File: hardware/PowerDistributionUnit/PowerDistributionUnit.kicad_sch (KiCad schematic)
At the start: 99 parts, among them J1 973582101, J2 973582100, J3 973582101, J4 973582100, Q1 SQJ141ELP, Q16 CSD18511Q5A, SW1 SW_Push, U1 TPS25983, U2 AD5258, U3 NUCLEO_LK43C

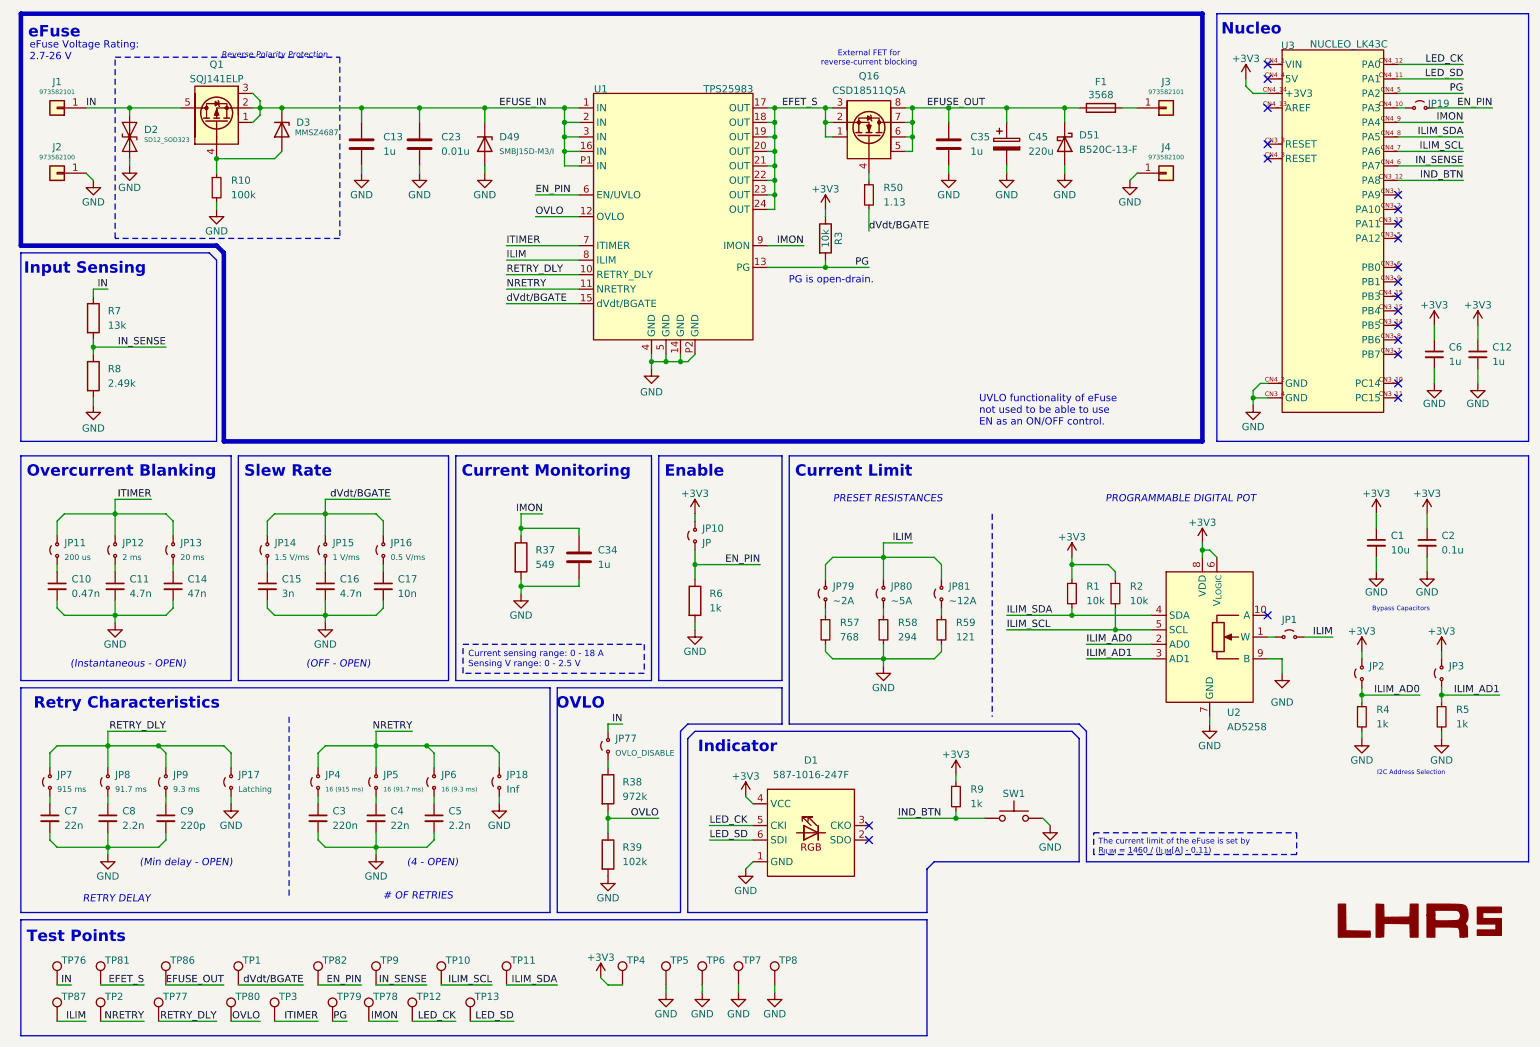
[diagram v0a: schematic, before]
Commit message: added separate power ground
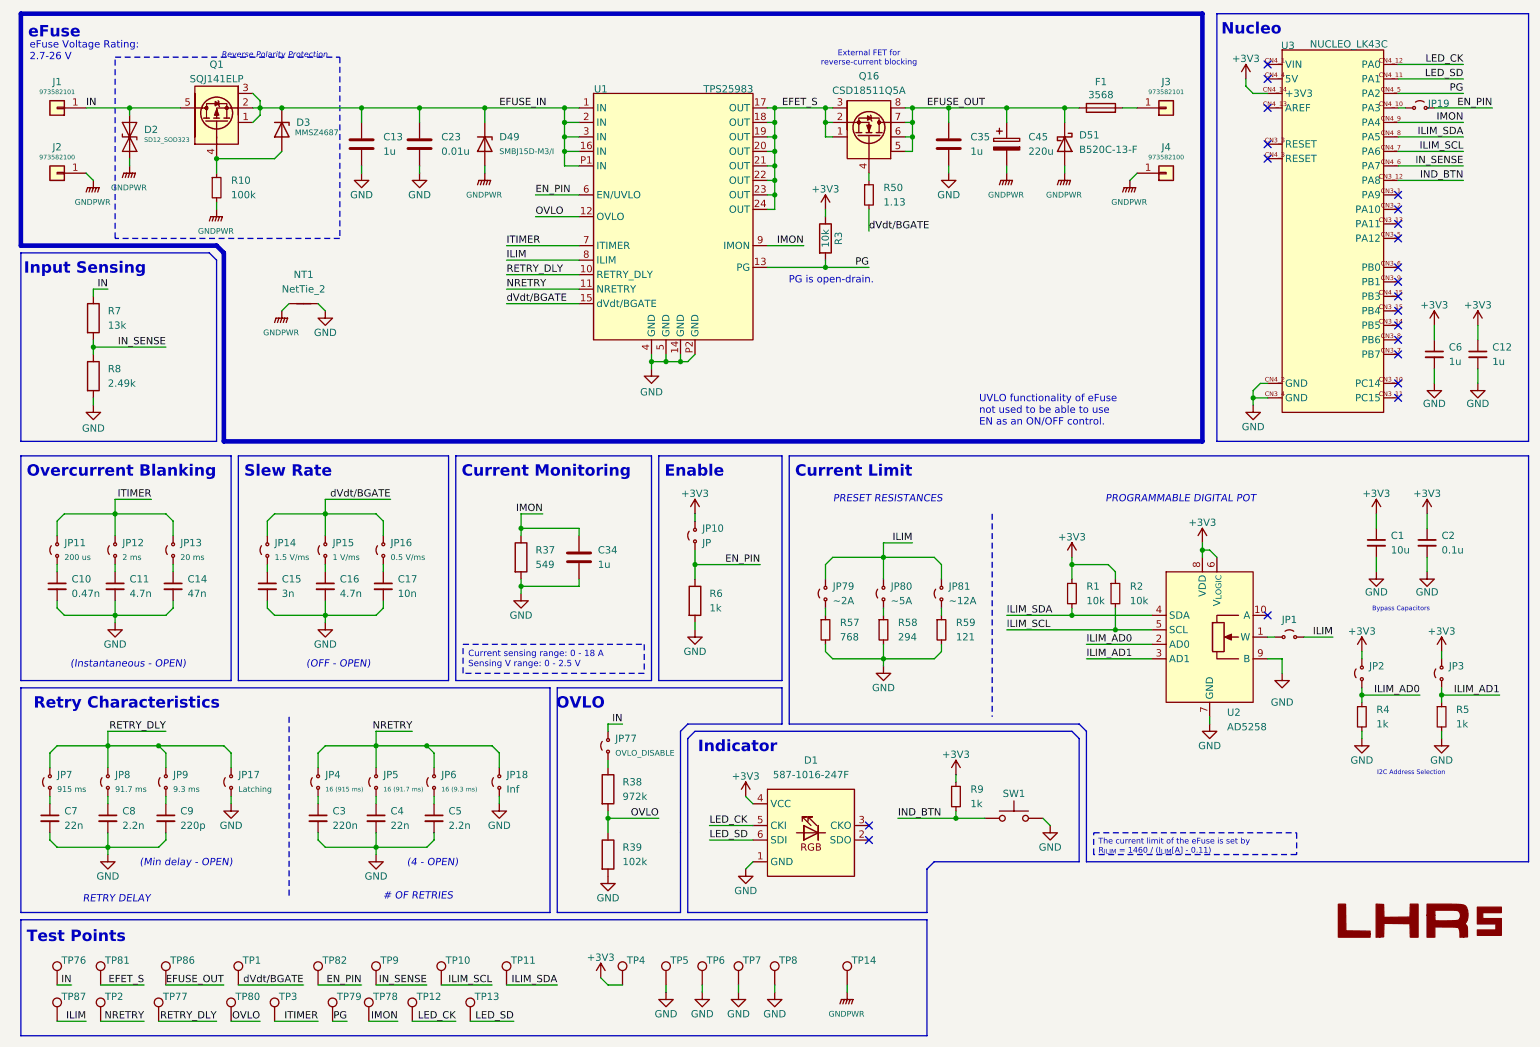
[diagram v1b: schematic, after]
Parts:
- added NT1: NetTie_2, symbol Device:NetTie_2
- added TP14: GND, symbol Connector:TestPoint
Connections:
- net GND: now also NT1.2; no longer C45.2, D2.1 (A1), D49.2 (A), D51.2 (A), J2.1 (Pin_1), J4.1 (Pin_1), R10.2
- new net GNDPWR: C45.2, D2.1 (A1), D49.2 (A), D51.2 (A), J2.1 (Pin_1), J4.1 (Pin_1), NT1.1, R10.2, TP14.1

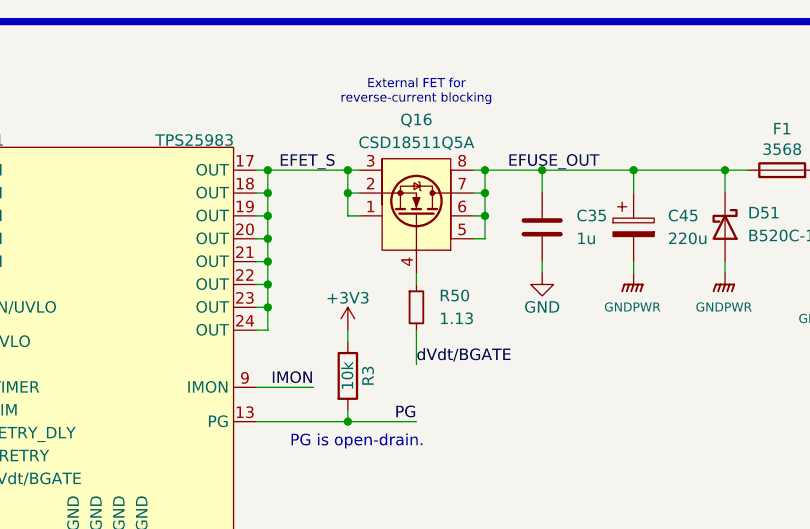
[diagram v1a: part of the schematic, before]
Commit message: footprint assignment, fixed rev current blocking fet symbol not matching generic footprint pins (replaced with generic mosfet symbol), fixed efuse pads pin numbers not lining up to footprint, added efuse footprint 3d model, added led footprint, imported footprints to pcb editor
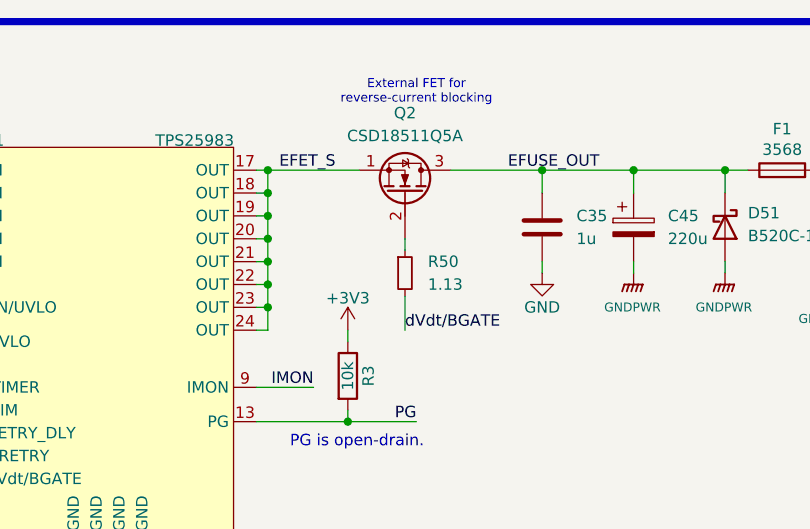
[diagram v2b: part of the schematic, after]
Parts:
- removed Q16: CSD18511Q5A, Package_SON:VSONP-8-1EP_5x6_P1.27mm, symbol PowerDistributionUnitLib:CSD18511Q5A
- added Q2: CSD18511Q5A, Package_SON:VSONP-8-1EP_5x6_P1.27mm, symbol Device:Q_NMOS_SGD
- C1, C10, C11, C12, C13, C14, C15, C16, C17, C2, C23, C3, C34, C35, C4, C5, C6, C7, C8, C9: footprint (none) -> Capacitor_SMD:C_0805_2012Metric
- C45: footprint Capacitor_SMD:CP_Elec_10x10.5 -> Capacitor_SMD:CP_Elec_10x12.6
- JP1, JP10, JP11, JP12, JP13, JP14, JP15, JP16, JP17, JP18, JP19, JP2, JP3, JP4, JP5, JP6, JP7, JP77, JP79, JP8, JP80, JP81, JP9: footprint (none) -> Connector_PinHeader_2.54mm:PinHeader_1x02_P2.54mm_Vertical
- NT1: footprint (none) -> NetTie:NetTie-2_SMD_Pad0.5mm
- R1, R10, R2, R3, R37, R38, R39, R4, R5, R50, R57, R58, R59, R6, R7, R8, R9: footprint (none) -> Resistor_SMD:R_0805_2012Metric
- TP1, TP2, TP3, TP76, TP77, TP78, TP79, TP80, TP81, TP82, TP86, TP87: footprint (none) -> TestPoint:TestPoint_Pad_D1.0mm
- TP10: value VIN -> ILIM_SCL; footprint (none) -> Connector_PinHeader_2.54mm:PinHeader_1x01_P2.54mm_Vertical
- TP11: value VIN -> ILIM_SDA; footprint (none) -> Connector_PinHeader_2.54mm:PinHeader_1x01_P2.54mm_Vertical
- TP12: value VIN -> LED_CK; footprint (none) -> Connector_PinHeader_2.54mm:PinHeader_1x01_P2.54mm_Vertical
- TP13: value VIN -> LED_SD; footprint (none) -> Connector_PinHeader_2.54mm:PinHeader_1x01_P2.54mm_Vertical
- TP14, TP4, TP5, TP6, TP7, TP8: footprint (none) -> Connector_PinHeader_2.54mm:PinHeader_1x01_P2.54mm_Vertical
- TP9: value VIN -> IN_SENSE; footprint (none) -> TestPoint:TestPoint_Pad_D1.0mm
- U3: footprint (none) -> PowerDistributionUnitLib:MODULE_NUCLEO-L432KC
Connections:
- net EFET_S: now also Q2.1 (S)
- net EFUSE_OUT: now also Q2.3 (D)
- net at R50.1: now also Q2.2 (G)
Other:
- moved on the sheet: R50

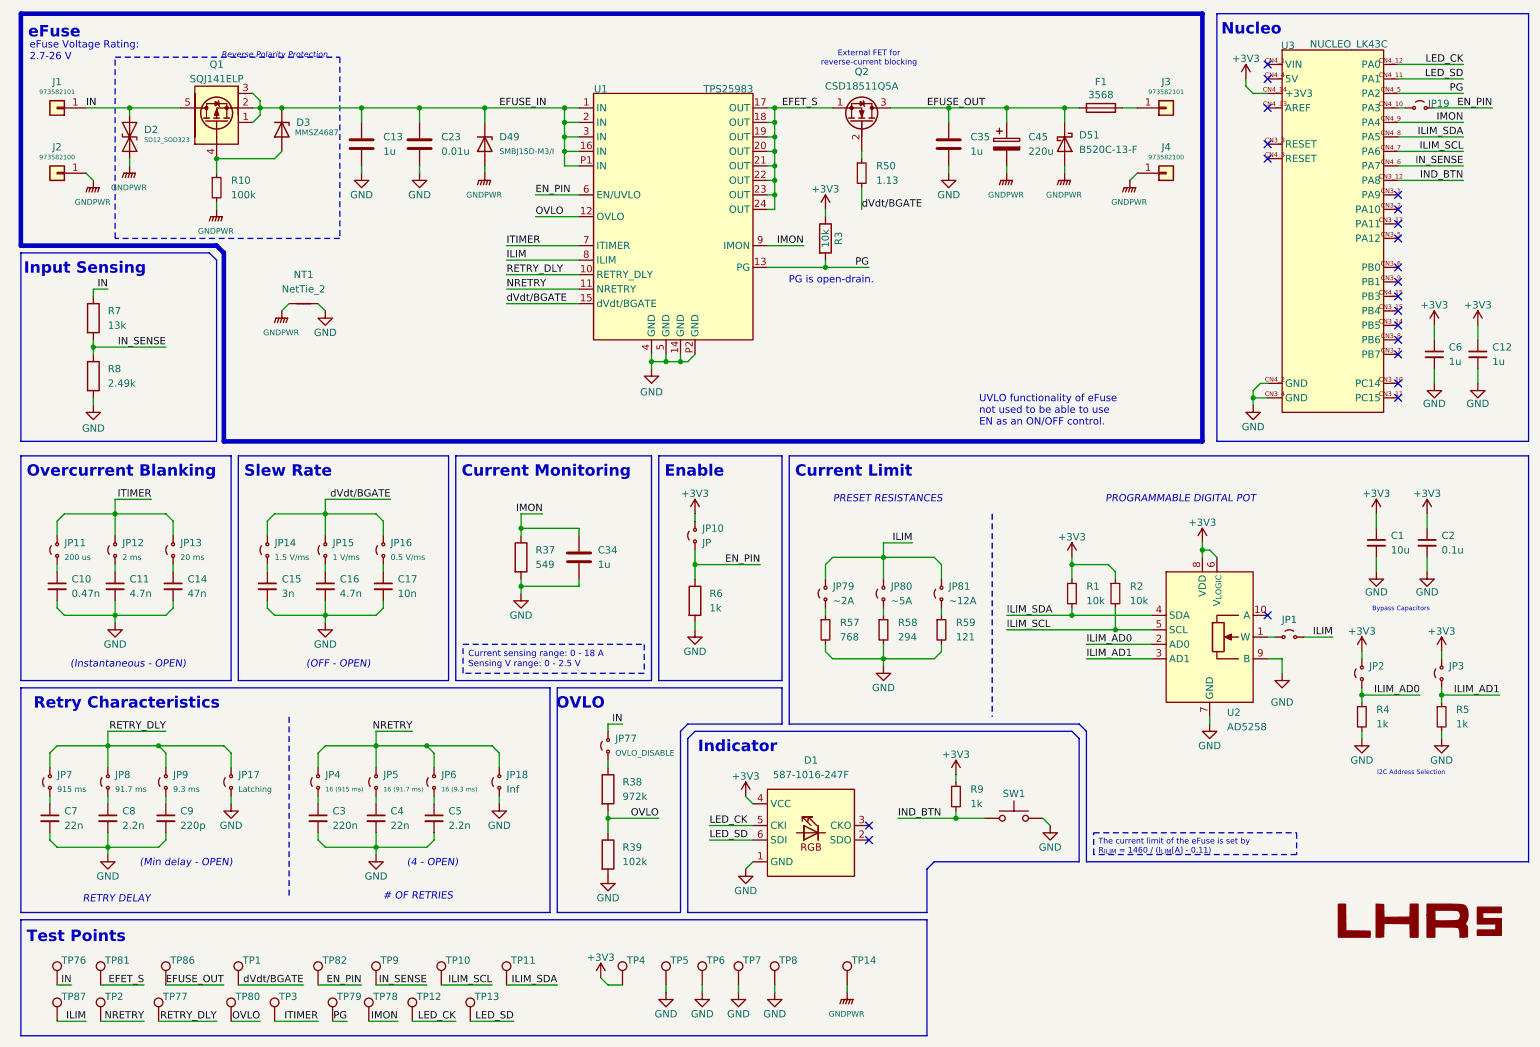
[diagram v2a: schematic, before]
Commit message: Finished placing components for layout, began traces
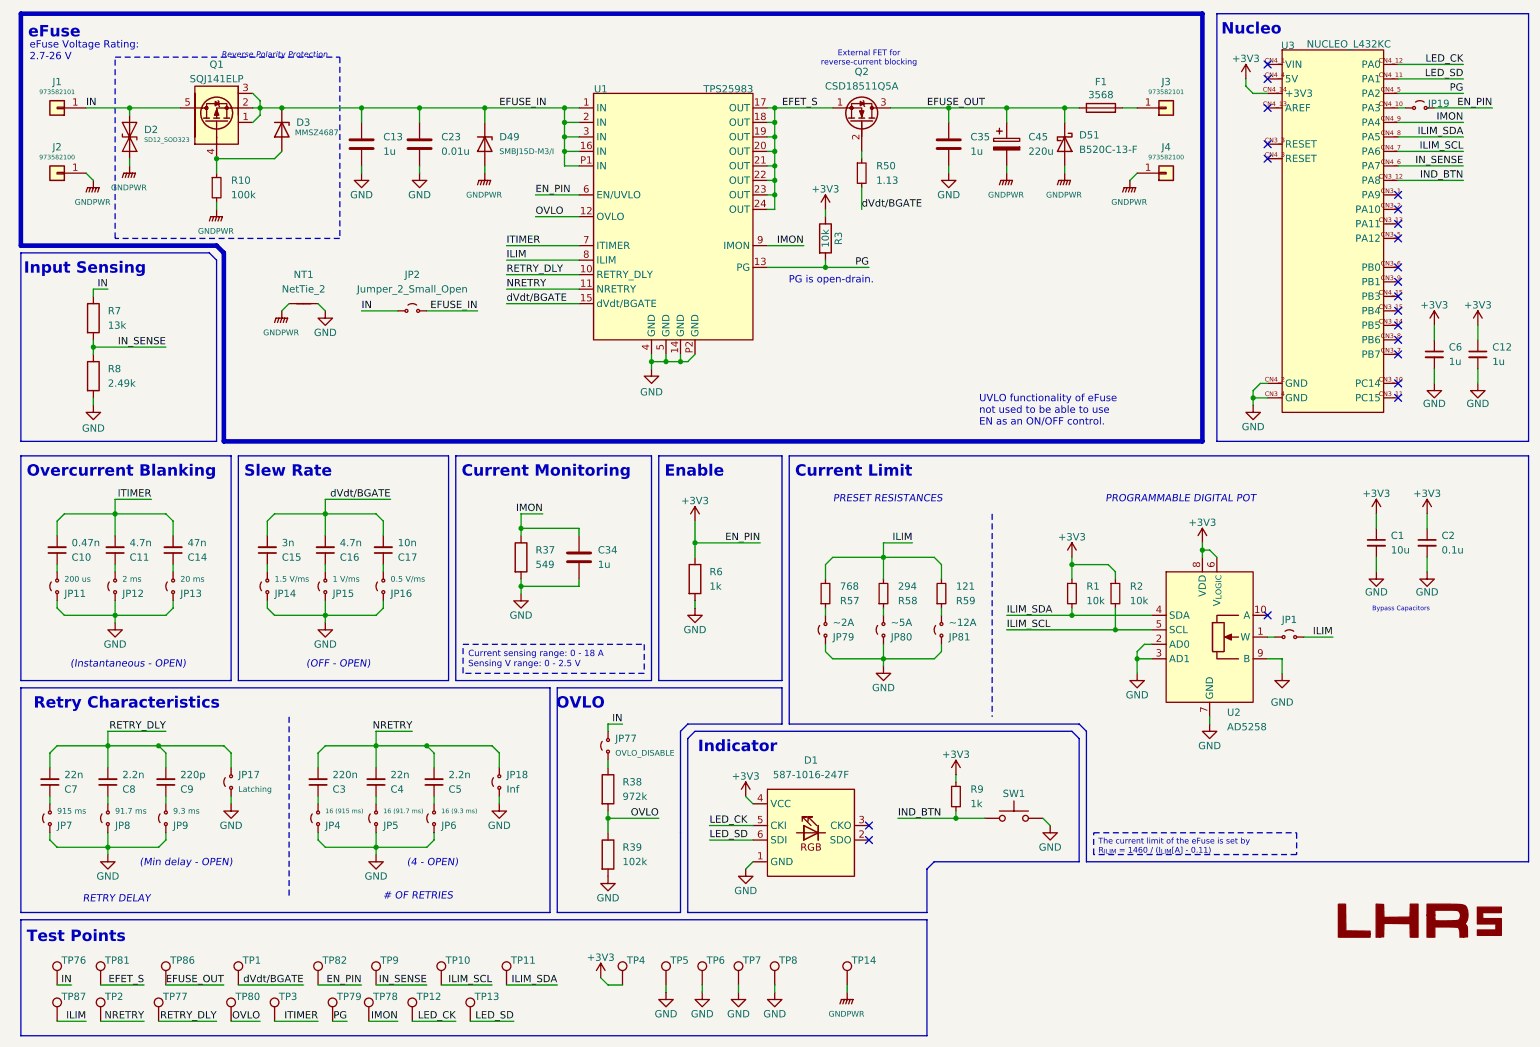
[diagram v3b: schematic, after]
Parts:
- removed JP10: JP, Connector_PinHeader_2.54mm:PinHeader_1x02_P2.54mm_Vertical, symbol Jumper:Jumper_2_Small_Open
- removed JP3: Jumper_2_Small_Open, Connector_PinHeader_2.54mm:PinHeader_1x02_P2.54mm_Vertical, symbol Jumper:Jumper_2_Small_Open
- removed R4, R5: 1k, Resistor_SMD:R_0805_2012Metric, symbol Device:R_Small
- U3: value NUCLEO_LK43C -> NUCLEO_L432KC
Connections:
- net EN_PIN is gone; now on net +3V3: JP19.2 (B), R6.1, TP82.1, U1.6 (EN/UVLO)
- net ILIM_AD1 is gone; now on net GND: U2.3 (AD1)
- net +3V3: no longer JP2.2 (B)
- net EFUSE_IN: now also JP2.2 (B)
- net GND: now also JP11.2 (B), JP12.2 (B), JP13.2 (B), JP14.2 (B), JP15.2 (B), JP16.2 (B), JP4.2 (B), JP5.2 (B), JP6.2 (B), JP7.2 (B), JP79.2 (B), JP8.2 (B), JP80.2 (B), JP81.2 (B), JP9.2 (B), U2.2 (AD0); no longer C10.2, C11.2, C14.2, C15.2, C16.2, C17.2, C3.2, C4.2, C5.2, C7.2, C8.2, C9.2, R57.2, R58.2, R59.2
- net ILIM: now also R57.2, R58.2, R59.2; no longer JP79.2 (B), JP80.2 (B), JP81.2 (B)
- net IN: now also JP2.1 (A)
- net ITIMER: now also C10.2, C11.2, C14.2; no longer JP11.2 (B), JP12.2 (B), JP13.2 (B)
- net NRETRY: now also C3.2, C4.2, C5.2; no longer JP4.2 (B), JP5.2 (B), JP6.2 (B)
- net RETRY_DLY: now also C7.2, C8.2, C9.2; no longer JP7.2 (B), JP8.2 (B), JP9.2 (B)
- net dVdt/BGATE: now also C15.2, C16.2, C17.2; no longer JP14.2 (B), JP15.2 (B), JP16.2 (B)
- removed net ILIM_AD0: JP2.1 (A), U2.2 (AD0)
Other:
- note removed: "I2C Address Selection"
- moved on the sheet: C10, C11, C14, C15, C16, C17, C3, C4, C5, C7, C8, C9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
